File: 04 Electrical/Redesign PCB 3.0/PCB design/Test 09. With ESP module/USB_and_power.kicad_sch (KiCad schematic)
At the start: 16 parts, among them J1 USB-C port, J3 Test connector, U2 SGM2212-3.3XKC3G/TR

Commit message: Routing PCB test 9
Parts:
- J3: footprint Project:PinHeader_1x04_P2.54mm_Horizontal -> Connector_PinHeader_2.54mm:PinHeader_1x06_P2.54mm_Vertical; symbol Connector:Conn_01x04_Pin -> Connector:Conn_01x06_Pin
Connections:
- new net Boiler 1: J3.6 (Pin_6)
- new net Boiler 2: J3.5 (Pin_5)

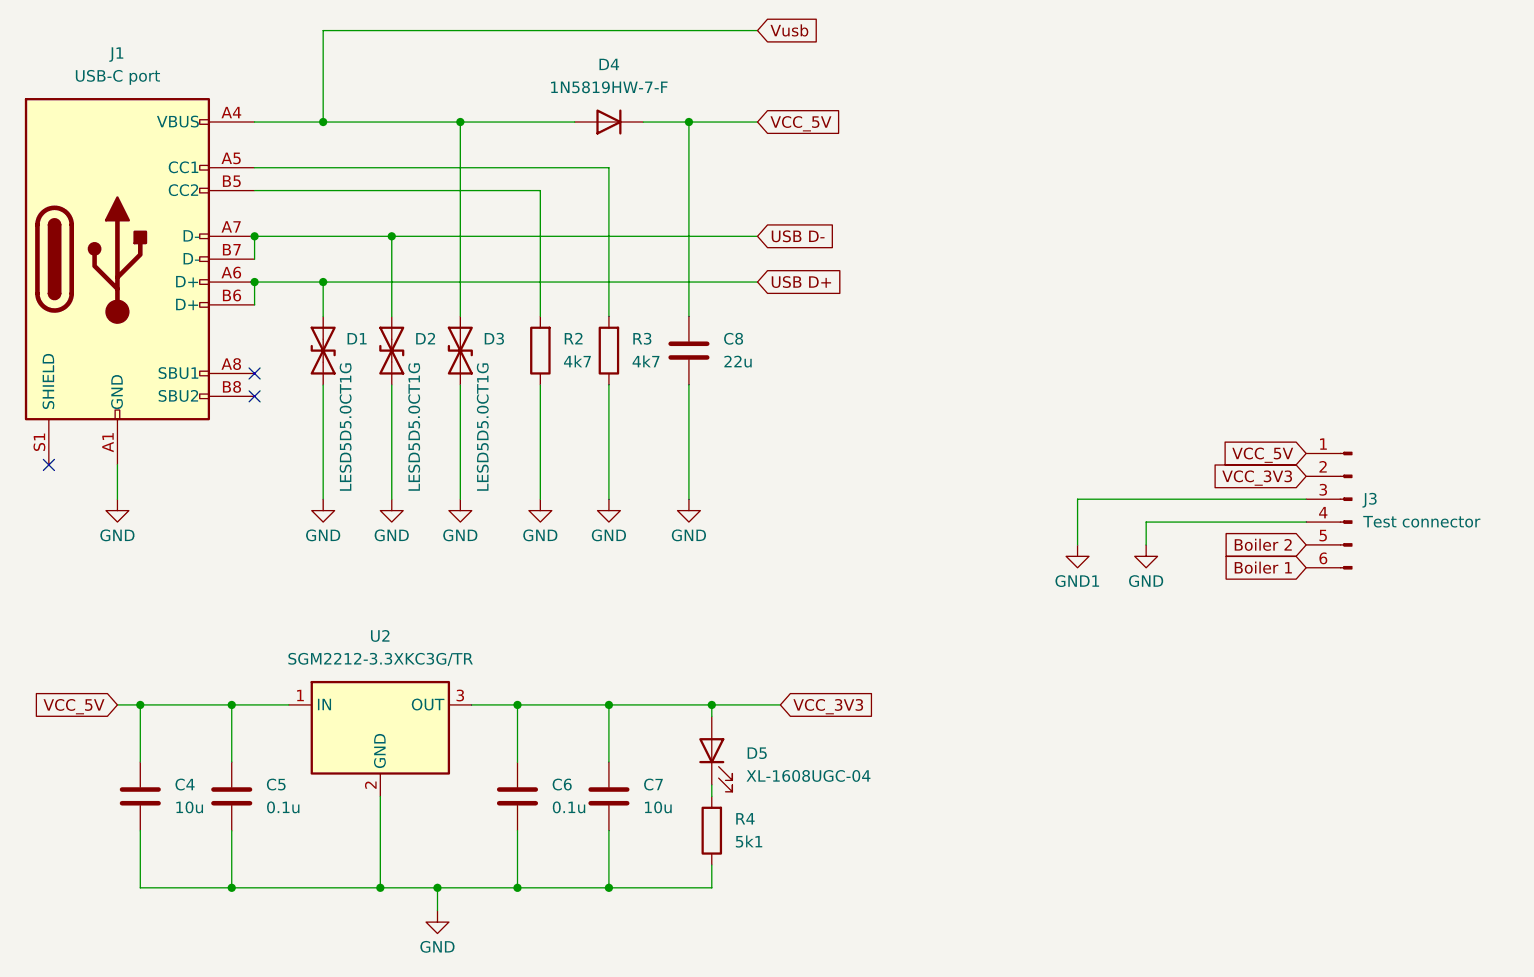
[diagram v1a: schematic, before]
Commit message: Logo added to PCB
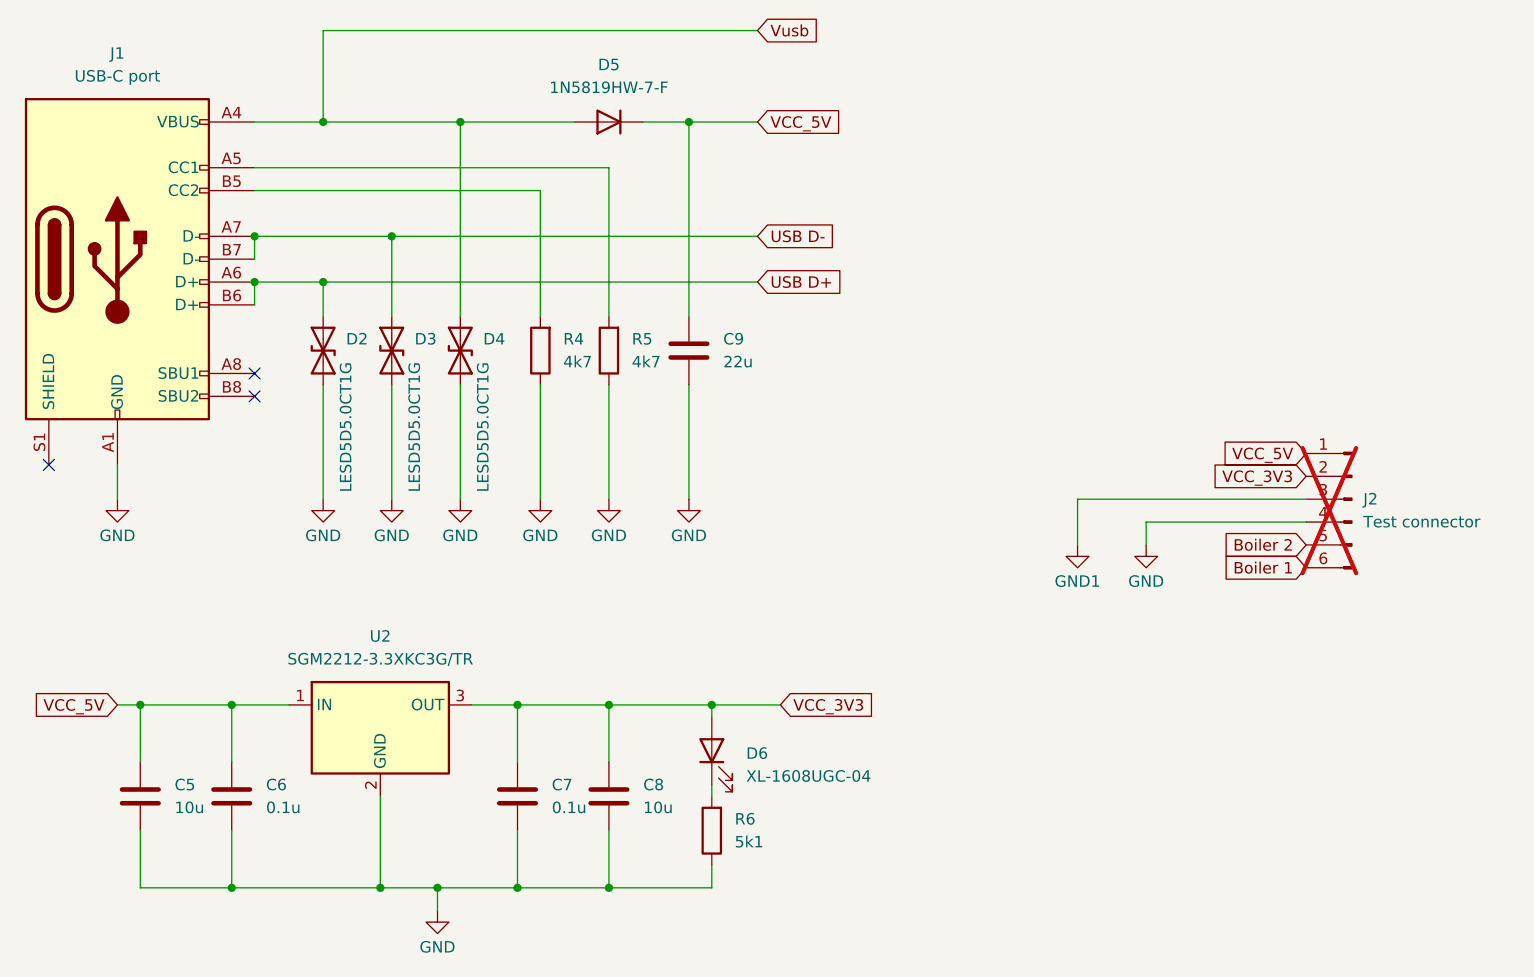
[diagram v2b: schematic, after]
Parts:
- J2: renamed from J3; now not fitted
- renumbered C4 to C5, C5 to C6, C6 to C7, C7 to C8, C8 to C9, D1 to D2, D2 to D3, D3 to D4, D4 to D5, D5 to D6, R2 to R4, R3 to R5, R4 to R6
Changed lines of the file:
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@@
 		(dnp no)
 		(fields_autoplaced yes)
-		(property "Reference" "D5"
+		(property "Reference" "D6"
 			(at 179.07 122.2374 90)
 			(effects
@@
 			(project "Test 09. With ESP module"
 				(path "/dee7d3c3-6abb-4cb3-8df4-3e3e37989a04/27673a3a-5c62-493b-b19a-59601297fae0"
-					(reference "D5")
+					(reference "D6")
 					(unit 1)
 				)
@@
 		(on_board yes)
 		(dnp no)
-		(property "Reference" "#PWR011"
+		(property "Reference" "#PWR013"
 			(at 163.83 100.33 0)
 			(effects
@@
 			(project "Test 09. With ESP module"
 				(path "/dee7d3c3-6abb-4cb3-8df4-3e3e37989a04/27673a3a-5c62-493b-b19a-59601297fae0"
-					(reference "#PWR011")
+					(reference "#PWR013")
 					(unit 1)
 				)
@@
 		(on_board yes)
 		(dnp no)
-		(property "Reference" "#PWR07"
+		(property "Reference" "#PWR09"
 			(at 139.7 100.33 0)
 			(effects
@@
 			(project "Test 09. With ESP module"
 				(path "/dee7d3c3-6abb-4cb3-8df4-3e3e37989a04/27673a3a-5c62-493b-b19a-59601297fae0"
-					(reference "#PWR07")
+					(reference "#PWR09")
 					(unit 1)
 				)
@@
 		(dnp no)
 		(fields_autoplaced yes)
-		(property "Reference" "C5"
+		(property "Reference" "C6"
 			(at 125.73 125.7299 0)
 			(effects
@@
 			(project "Test 09. With ESP module"
 				(path "/dee7d3c3-6abb-4cb3-8df4-3e3e37989a04/27673a3a-5c62-493b-b19a-59601297fae0"
-					(reference "C5")
+					(reference "C6")
 					(unit 1)
 				)
@@
 		(on_board yes)
 		(dnp no)
-		(property "Reference" "D1"
+		(property "Reference" "D2"
 			(at 134.62 76.1999 90)
 			(effects
@@
 			(project "Test 09. With ESP module"
 				(path "/dee7d3c3-6abb-4cb3-8df4-3e3e37989a04/27673a3a-5c62-493b-b19a-59601297fae0"
-					(reference "D1")
+					(reference "D2")
 					(unit 1)
 				)
@@
 		(dnp no)
 		(fields_autoplaced yes)
-		(property "Reference" "R2"
+		(property "Reference" "R4"
 			(at 158.75 76.1999 0)
 			(effects
@@
 			(project "Test 09. With ESP module"
 				(path "/dee7d3c3-6abb-4cb3-8df4-3e3e37989a04/27673a3a-5c62-493b-b19a-59601297fae0"
-					(reference "R2")
+					(reference "R4")
 					(unit 1)
 				)
@@
 		(dnp no)
 		(fields_autoplaced yes)
-		(property "Reference" "C8"
+		(property "Reference" "C9"
 			(at 176.53 76.1999 0)
 			(effects
@@
 			(project "Test 09. With ESP module"
 				(path "/dee7d3c3-6abb-4cb3-8df4-3e3e37989a04/27673a3a-5c62-493b-b19a-59601297fae0"
-					(reference "C8")
+					(reference "C9")
 					(unit 1)
 				)
@@
 		(dnp no)
 		(fields_autoplaced yes)
-		(property "Reference" "C7"
+		(property "Reference" "C8"
 			(at 167.64 125.7299 0)
 			(effects
@@
 			(project "Test 09. With ESP module"
 				(path "/dee7d3c3-6abb-4cb3-8df4-3e3e37989a04/27673a3a-5c62-493b-b19a-59601297fae0"
-					(reference "C7")
+					(reference "C8")
 					(unit 1)
 				)
@@
 		(dnp no)
 		(fields_autoplaced yes)
-		(property "Reference" "R4"
+		(property "Reference" "R6"
 			(at 177.8 129.5399 0)
 			(effects
@@
 			(project "Test 09. With ESP module"
 				(path "/dee7d3c3-6abb-4cb3-8df4-3e3e37989a04/27673a3a-5c62-493b-b19a-59601297fae0"
-					(reference "R4")
+					(reference "R6")
 					(unit 1)
 				)
@@
 		(on_board yes)
 		(dnp no)
-		(property "Reference" "#PWR08"
+		(property "Reference" "#PWR010"
 			(at 144.78 146.05 0)
 			(effects
@@
 			(project "Test 09. With ESP module"
 				(path "/dee7d3c3-6abb-4cb3-8df4-3e3e37989a04/27673a3a-5c62-493b-b19a-59601297fae0"
-					(reference "#PWR08")
+					(reference "#PWR010")
 					(unit 1)
 				)
@@
 		(on_board yes)
 		(dnp no)
-		(property "Reference" "#PWR010"
+		(property "Reference" "#PWR012"
 			(at 156.21 100.33 0)
 			(effects
@@
 			(project "Test 09. With ESP module"
 				(path "/dee7d3c3-6abb-4cb3-8df4-3e3e37989a04/27673a3a-5c62-493b-b19a-59601297fae0"
-					(reference "#PWR010")
+					(reference "#PWR012")
 					(unit 1)
 				)
@@
 		(on_board yes)
 		(dnp no)
-		(property "Reference" "#PWR05"
+		(property "Reference" "#PWR07"
 			(at 109.22 100.33 0)
 			(effects
@@
 			(project "Test 09. With ESP module"
 				(path "/dee7d3c3-6abb-4cb3-8df4-3e3e37989a04/27673a3a-5c62-493b-b19a-59601297fae0"
-					(reference "#PWR05")
+					(reference "#PWR07")
 					(unit 1)
 				)
@@
 		(dnp no)
 		(fields_autoplaced yes)
-		(property "Reference" "C4"
+		(property "Reference" "C5"
 			(at 115.57 125.7299 0)
 			(effects
@@
 			(project "Test 09. With ESP module"
 				(path "/dee7d3c3-6abb-4cb3-8df4-3e3e37989a04/27673a3a-5c62-493b-b19a-59601297fae0"
-					(reference "C4")
+					(reference "C5")
 					(unit 1)
 				)
@@
 		(on_board yes)
 		(dnp no)
-		(property "Reference" "#PWR034"
+		(property "Reference" "#PWR016"
 			(at 223.52 105.41 0)
 			(effects
@@
 			(project "Test 09. With ESP module"
 				(path "/dee7d3c3-6abb-4cb3-8df4-3e3e37989a04/27673a3a-5c62-493b-b19a-59601297fae0"
-					(reference "#PWR034")
+					(reference "#PWR016")
 					(unit 1)
 				)
@@
 		(dnp no)
 		(fields_autoplaced yes)
-		(property "Reference" "C6"
+		(property "Reference" "C7"
 			(at 157.48 125.7299 0)
 			(effects
@@
 			(project "Test 09. With ESP module"
 				(path "/dee7d3c3-6abb-4cb3-8df4-3e3e37989a04/27673a3a-5c62-493b-b19a-59601297fae0"
-					(reference "C6")
+					(reference "C7")
 					(unit 1)
 				)
@@
 		(on_board yes)
 		(dnp no)
-		(property "Reference" "#PWR033"
+		(property "Reference" "#PWR015"
 			(at 215.9 105.41 0)
 			(effects
@@
 			(project "Test 09. With ESP module"
 				(path "/dee7d3c3-6abb-4cb3-8df4-3e3e37989a04/27673a3a-5c62-493b-b19a-59601297fae0"
-					(reference "#PWR033")
+					(reference "#PWR015")
 					(unit 1)
 				)
@@
 		(dnp no)
 		(fields_autoplaced yes)
-		(property "Reference" "R3"
+		(property "Reference" "R5"
 			(at 166.37 76.1999 0)
 			(effects
@@
 			(project "Test 09. With ESP module"
 				(path "/dee7d3c3-6abb-4cb3-8df4-3e3e37989a04/27673a3a-5c62-493b-b19a-59601297fae0"
-					(reference "R3")
+					(reference "R5")
 					(unit 1)
 				)
@@
 		(dnp no)
 		(fields_autoplaced yes)
-		(property "Reference" "D4"
+		(property "Reference" "D5"
 			(at 163.83 45.72 0)
 			(effects
@@
 			(project "Test 09. With ESP module"
 				(path "/dee7d3c3-6abb-4cb3-8df4-3e3e37989a04/27673a3a-5c62-493b-b19a-59601297fae0"
-					(reference "D4")
+					(reference "D5")
 					(unit 1)
 				)
@@
 		(on_board yes)
 		(dnp no)
-		(property "Reference" "D2"
+		(property "Reference" "D3"
 			(at 142.24 76.1999 90)
 			(effects
@@
 			(project "Test 09. With ESP module"
 				(path "/dee7d3c3-6abb-4cb3-8df4-3e3e37989a04/27673a3a-5c62-493b-b19a-59601297fae0"
-					(reference "D2")
+					(reference "D3")
 					(unit 1)
 				)
@@
 		(on_board yes)
 		(dnp no)
-		(property "Reference" "#PWR012"
+		(property "Reference" "#PWR014"
 			(at 172.72 100.33 0)
 			(effects
@@
 			(project "Test 09. With ESP module"
 				(path "/dee7d3c3-6abb-4cb3-8df4-3e3e37989a04/27673a3a-5c62-493b-b19a-59601297fae0"
-					(reference "#PWR012")
+					(reference "#PWR014")
 					(unit 1)
 				)
@@
 		(on_board yes)
 		(dnp no)
-		(property "Reference" "#PWR06"
+		(property "Reference" "#PWR08"
 			(at 132.08 100.33 0)
 			(effects
@@
 			(project "Test 09. With ESP module"
 				(path "/dee7d3c3-6abb-4cb3-8df4-3e3e37989a04/27673a3a-5c62-493b-b19a-59601297fae0"
-					(reference "#PWR06")
+					(reference "#PWR08")
 					(unit 1)
 				)
@@
 		(on_board yes)
 		(dnp no)
-		(property "Reference" "D3"
+		(property "Reference" "D4"
 			(at 149.86 76.1999 90)
 			(effects
@@
 			(project "Test 09. With ESP module"
 				(path "/dee7d3c3-6abb-4cb3-8df4-3e3e37989a04/27673a3a-5c62-493b-b19a-59601297fae0"
-					(reference "D3")
+					(reference "D4")
 					(unit 1)
 				)
@@
 		(in_bom yes)
 		(on_board yes)
-		(dnp no)
+		(dnp yes)
 		(fields_autoplaced yes)
-		(property "Reference" "J3"
+		(property "Reference" "J2"
 			(at 247.65 93.9799 0)
 			(effects
@@
 			(project ""
 				(path "/dee7d3c3-6abb-4cb3-8df4-3e3e37989a04/27673a3a-5c62-493b-b19a-59601297fae0"
-					(reference "J3")
+					(reference "J2")
 					(unit 1)
 				)
@@
 		(on_board yes)
 		(dnp no)
-		(property "Reference" "#PWR09"
+		(property "Reference" "#PWR011"
 			(at 147.32 100.33 0)
 			(effects
@@
 			(project "Test 09. With ESP module"
 				(path "/dee7d3c3-6abb-4cb3-8df4-3e3e37989a04/27673a3a-5c62-493b-b19a-59601297fae0"
-					(reference "#PWR09")
-					(unit 1)
-				)
+					(reference "#PWR011")
+					(unit 1)
+				)

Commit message: As ordered at JLCPCB
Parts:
- removed J2: Test connector, Connector_PinHeader_2.54mm:PinHeader_1x06_P2.54mm_Vertical, symbol Connector:Conn_01x06_Pin
- added TP1: 5V, TestPoint:TestPoint_Keystone_5015_Micro-Minature, symbol Connector:TestPoint
- added TP2: 3V3, TestPoint:TestPoint_Keystone_5015_Micro-Minature, symbol Connector:TestPoint
- added TP3: GND1, TestPoint:TestPoint_Keystone_5015_Micro-Minature, symbol Connector:TestPoint
- added TP4: GND, TestPoint:TestPoint_Keystone_5015_Micro-Minature, symbol Connector:TestPoint
- added TP5: opnthm, TestPoint:TestPoint_Keystone_5015_Micro-Minature, symbol Connector:TestPoint
- added TP6: B1, TestPoint:TestPoint_Keystone_5015_Micro-Minature, symbol Connector:TestPoint
- added TP7: B2, TestPoint:TestPoint_Keystone_5015_Micro-Minature, symbol Connector:TestPoint
- C5, C8: LCSC Part #  C15525 -> C15525
- D2, D3, D4: value LESD5D5.0CT1G -> BSD5C051L; LCSC Part #  C383211 -> C151983
- U2: value SGM2212-3.3XKC3G/TR -> UZ1086L-33-TN3-R; footprint Package_TO_SOT_SMD:SOT-223-3_TabPin2 -> Package_TO_SOT_SMD:TO-252-2; LCSC Part #  C3294699 -> C125862
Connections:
- net Boiler 1: now also TP6.1
- net Boiler 2: now also TP7.1
- net GND: now also TP4.1
- net GND1: now also TP3.1
- net VCC_3V3: now also TP2.1
- net VCC_5V: now also TP1.1
- new net boiler: TP5.1
